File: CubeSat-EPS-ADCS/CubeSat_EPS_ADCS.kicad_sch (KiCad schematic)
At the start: 18 parts, among them J1 Conn_01x02_Pin, J2 Conn_01x03_Pin, J3 Conn_01x08_Pin, J4 Conn_01x02_Pin, J5 Screw_Terminal_01x02, J6 Screw_Terminal_01x02, J7 Screw_Terminal_01x02, U1 DRV8833 Module, U2 DRV8833 Module, U4 Buck_LM2596

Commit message: Mostly fine tuning the boards, also added capacitor for battery ADC
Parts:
- removed R1, R2, R3, R4, R5, R6: 10K, Resistor_THT:R_Axial_DIN0207_L6.3mm_D2.5mm_P7.62mm_Horizontal, symbol Device:R
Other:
- note removed: "PULL DOWN RESISTORS"

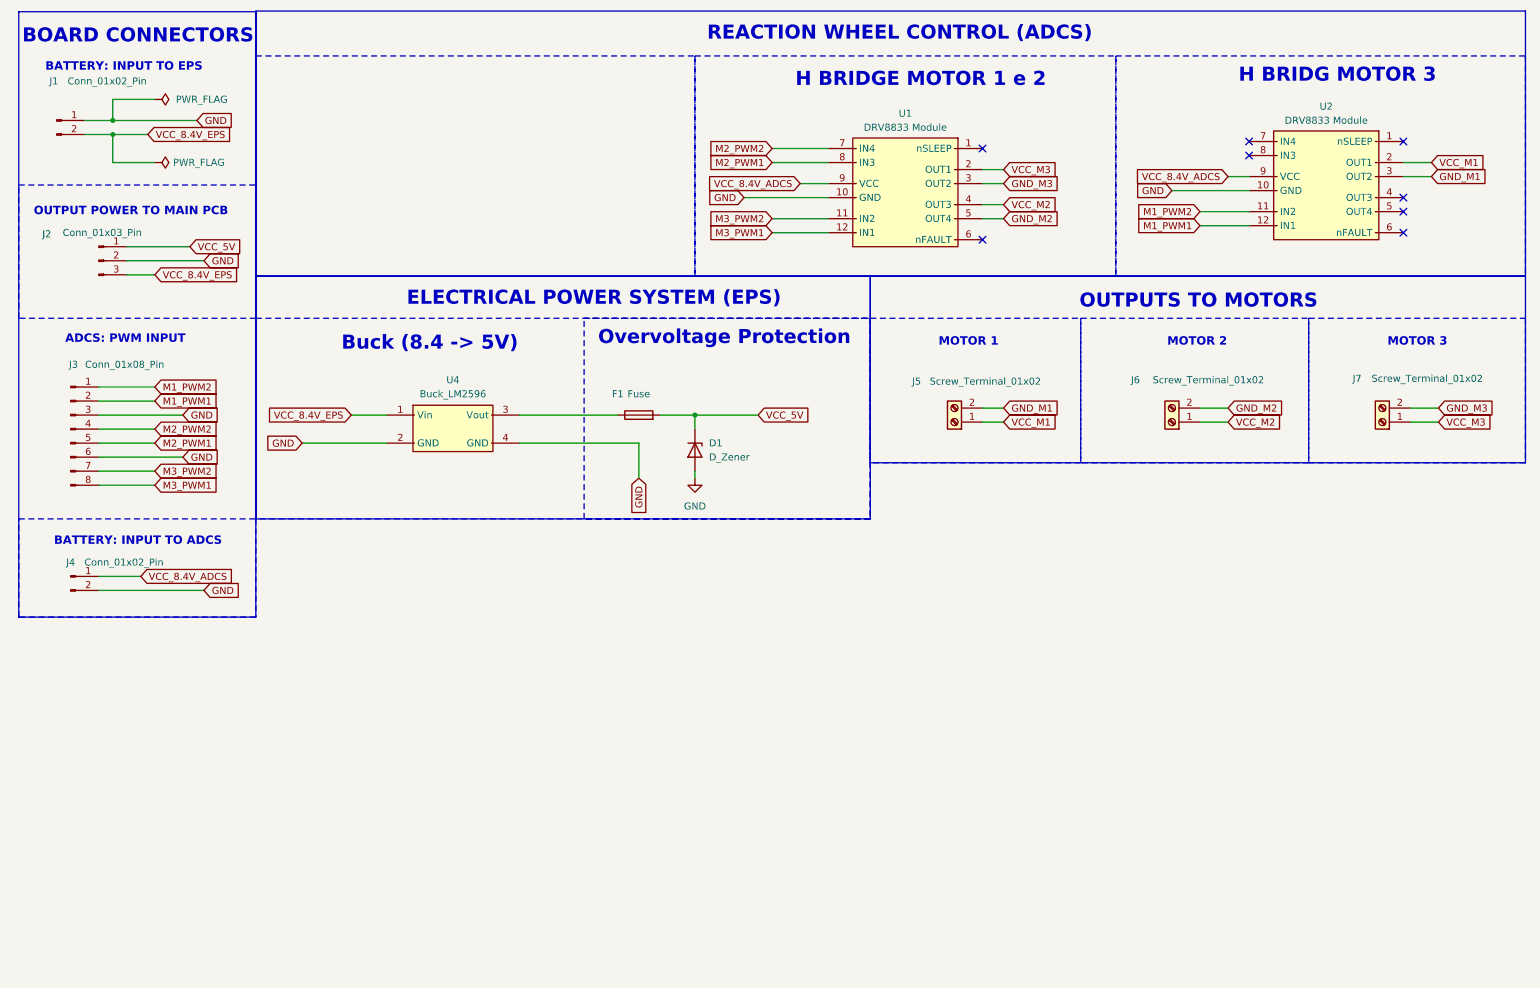
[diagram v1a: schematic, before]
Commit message: Changing the size of all traces to fit the 1 mm requirement of the draft PCB
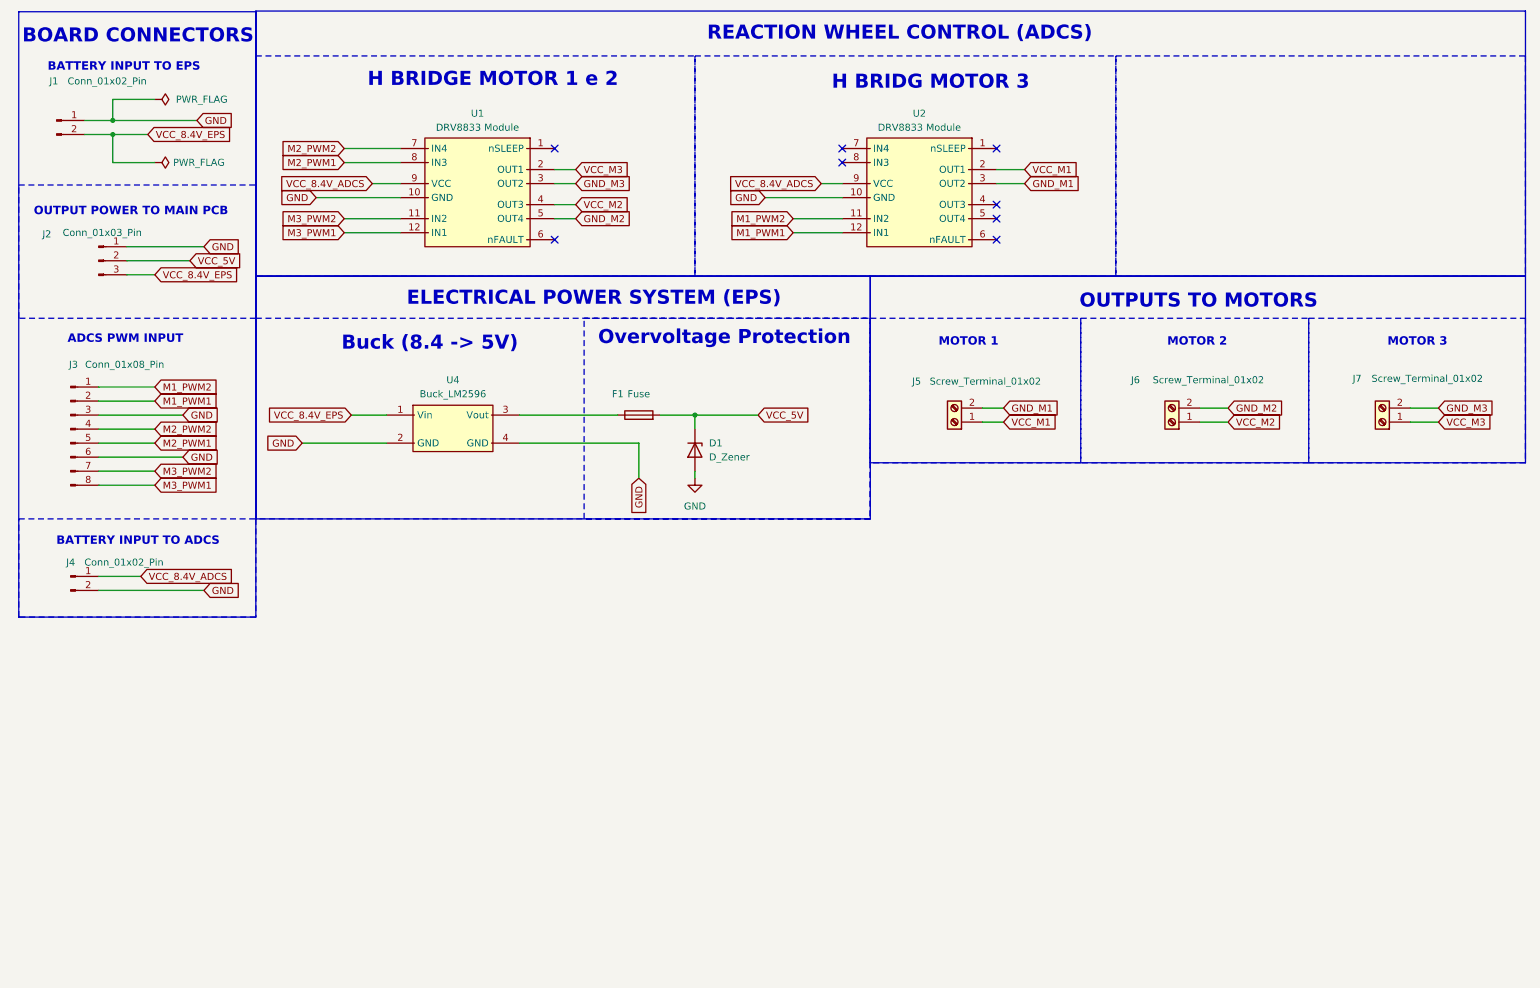
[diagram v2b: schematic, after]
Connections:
- net GND: now also J2.1 (Pin_1); no longer J2.2 (Pin_2)
- net VCC_5V: now also J2.2 (Pin_2); no longer J2.1 (Pin_1)
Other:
- note added: "ADCS PWM INPUT"
- note added: "BATTERY INPUT TO ADCS"
- note added: "BATTERY INPUT TO EPS"
- note removed: "ADCS: PWM INPUT"
- note removed: "BATTERY: INPUT TO ADCS"
- note removed: "BATTERY: INPUT TO EPS"
- moved on the sheet: U1, U2

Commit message: final version of the 3 PCBs, minor size changes for the protoypes
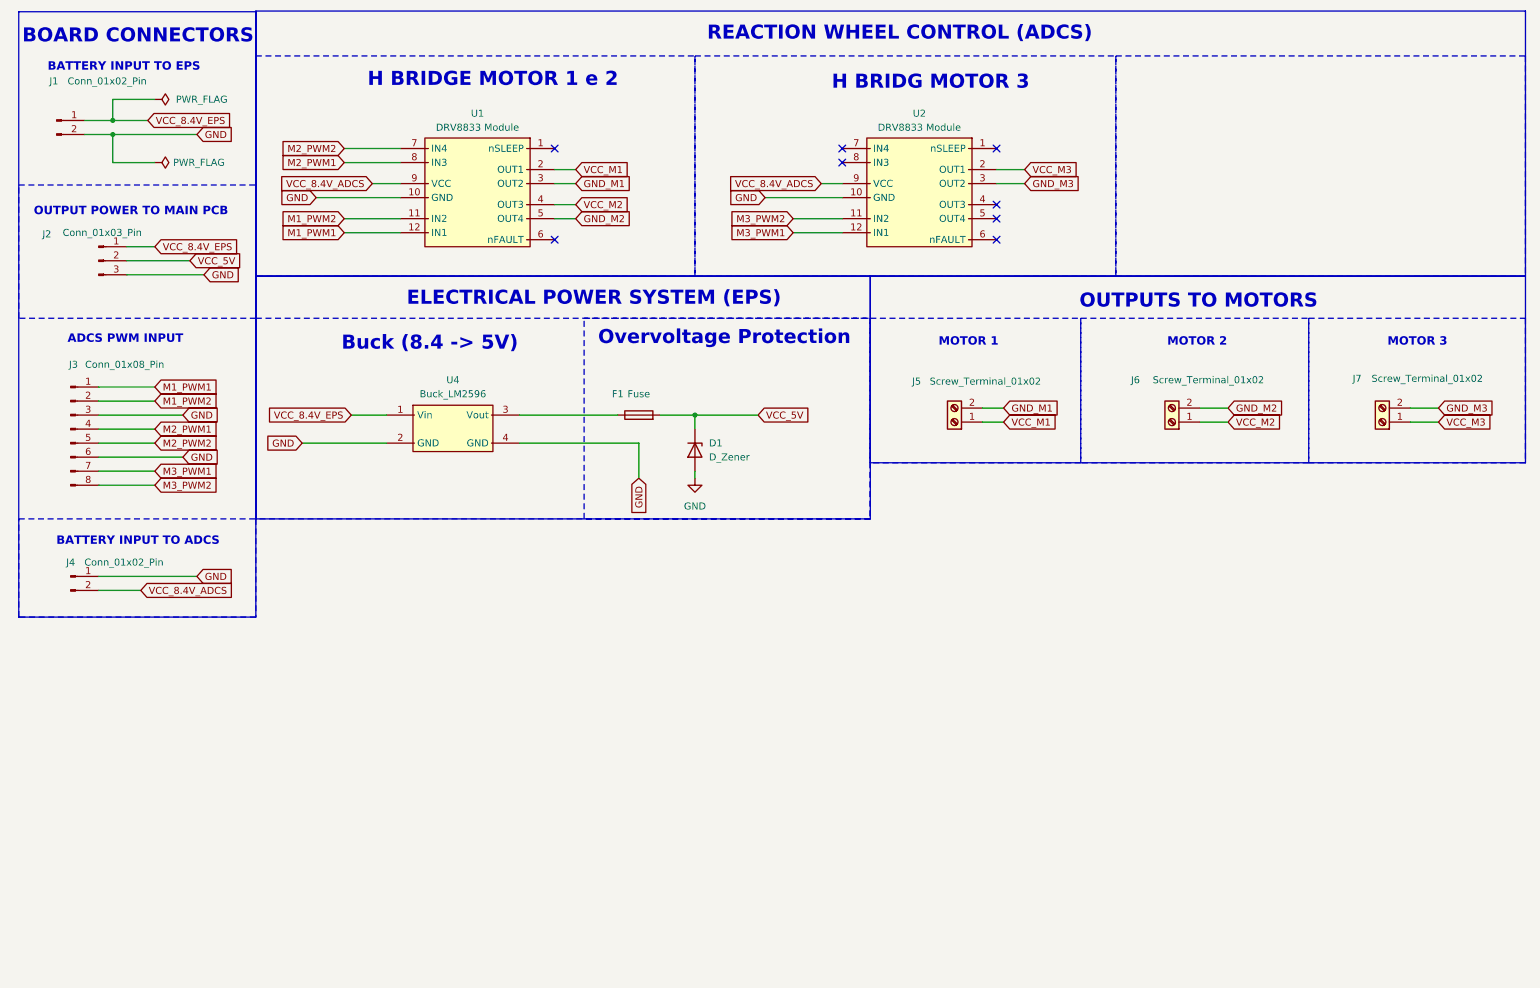
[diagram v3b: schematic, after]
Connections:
- net GND: now also J1.2 (Pin_2), J2.3 (Pin_3), J4.1 (Pin_1); no longer J1.1 (Pin_1), J2.1 (Pin_1), J4.2 (Pin_2)
- net GND_M1: now also U1.3 (OUT2); no longer U2.3 (OUT2)
- net GND_M3: now also U2.3 (OUT2); no longer U1.3 (OUT2)
- net M1_PWM1: now also J3.1 (Pin_1), U1.12 (IN1); no longer J3.2 (Pin_2), U2.12 (IN1)
- net M1_PWM2: now also J3.2 (Pin_2), U1.11 (IN2); no longer J3.1 (Pin_1), U2.11 (IN2)
- net M2_PWM1: now also J3.4 (Pin_4); no longer J3.5 (Pin_5)
- net M2_PWM2: now also J3.5 (Pin_5); no longer J3.4 (Pin_4)
- net M3_PWM1: now also J3.7 (Pin_7), U2.12 (IN1); no longer J3.8 (Pin_8), U1.12 (IN1)
- net M3_PWM2: now also J3.8 (Pin_8), U2.11 (IN2); no longer J3.7 (Pin_7), U1.11 (IN2)
- net VCC_8.4V_ADCS: now also J4.2 (Pin_2); no longer J4.1 (Pin_1)
- net VCC_8.4V_EPS: now also J1.1 (Pin_1), J2.1 (Pin_1); no longer J1.2 (Pin_2), J2.3 (Pin_3)
- net VCC_M1: now also U1.2 (OUT1); no longer U2.2 (OUT1)
- net VCC_M3: now also U2.2 (OUT1); no longer U1.2 (OUT1)

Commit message: add new drill format
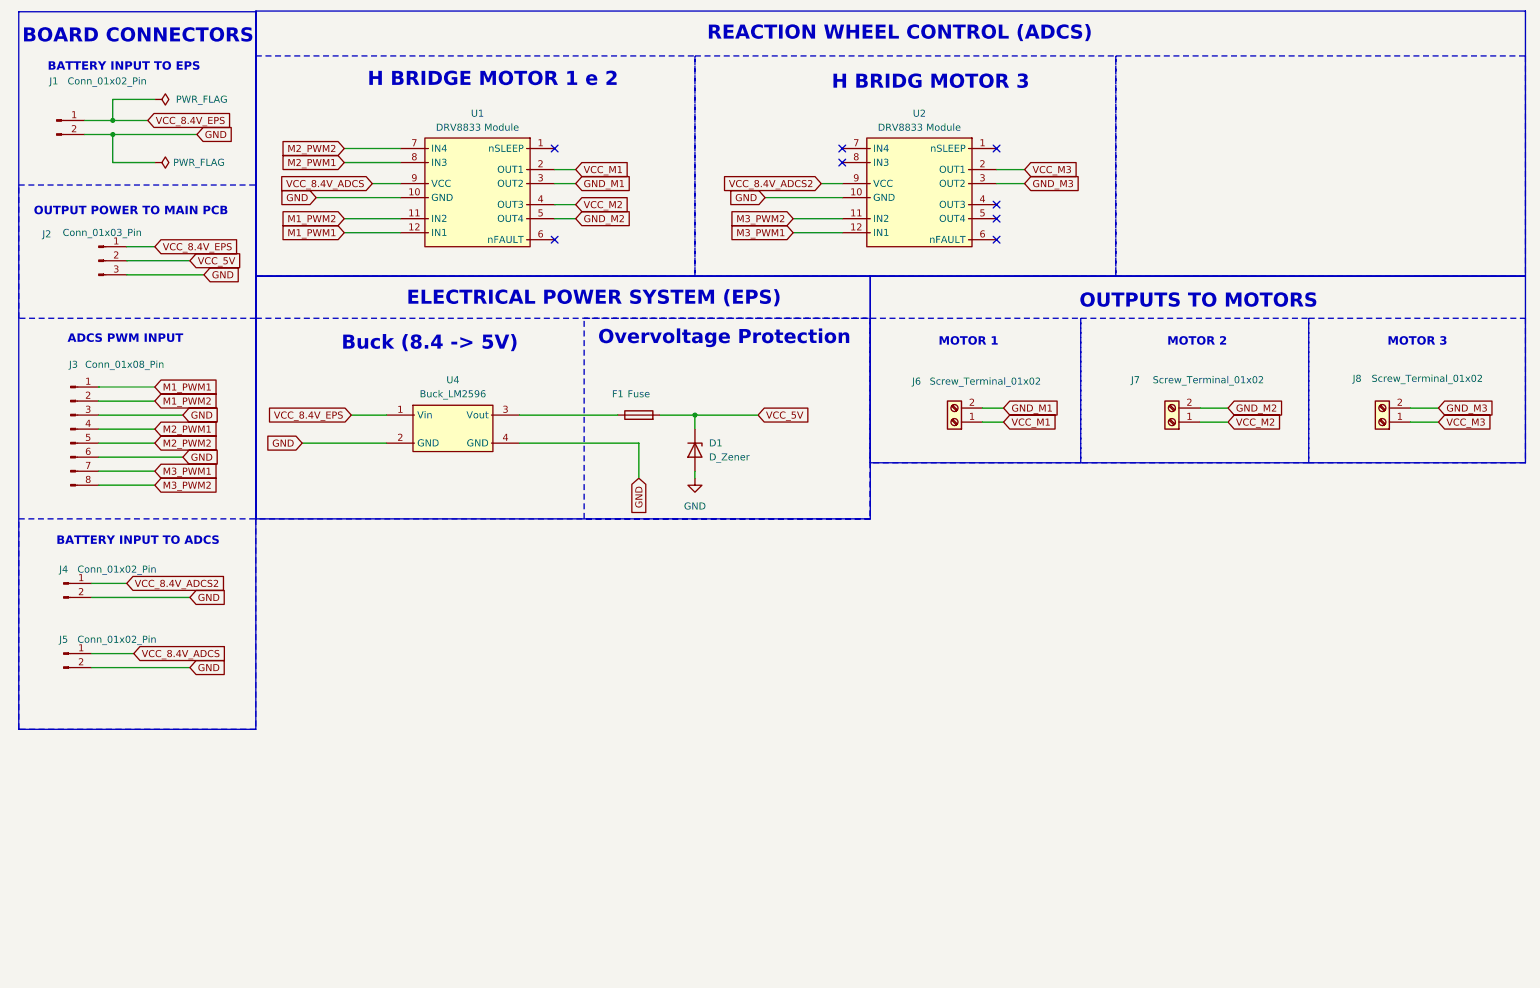
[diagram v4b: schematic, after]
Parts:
- added J4: Conn_01x02_Pin, Connector_JST:JST_EH_B2B-EH-A_1x02_P2.50mm_Vertical, symbol Connector:Conn_01x02_Pin
- renumbered J4 to J5, J5 to J6, J6 to J7, J7 to J8
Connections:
- net GND: now also J5.2 (Pin_2), J4.2 (Pin_2); no longer J5.1 (Pin_1)
- net VCC_8.4V_ADCS: now also J5.1 (Pin_1); no longer J5.2 (Pin_2), U2.9 (VCC)
- new net VCC_8.4V_ADCS2: J4.1 (Pin_1), U2.9 (VCC)
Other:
- moved on the sheet: J5

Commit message: final changes in ALL 3 pcbs: mounting wholes config, and a few connector changes
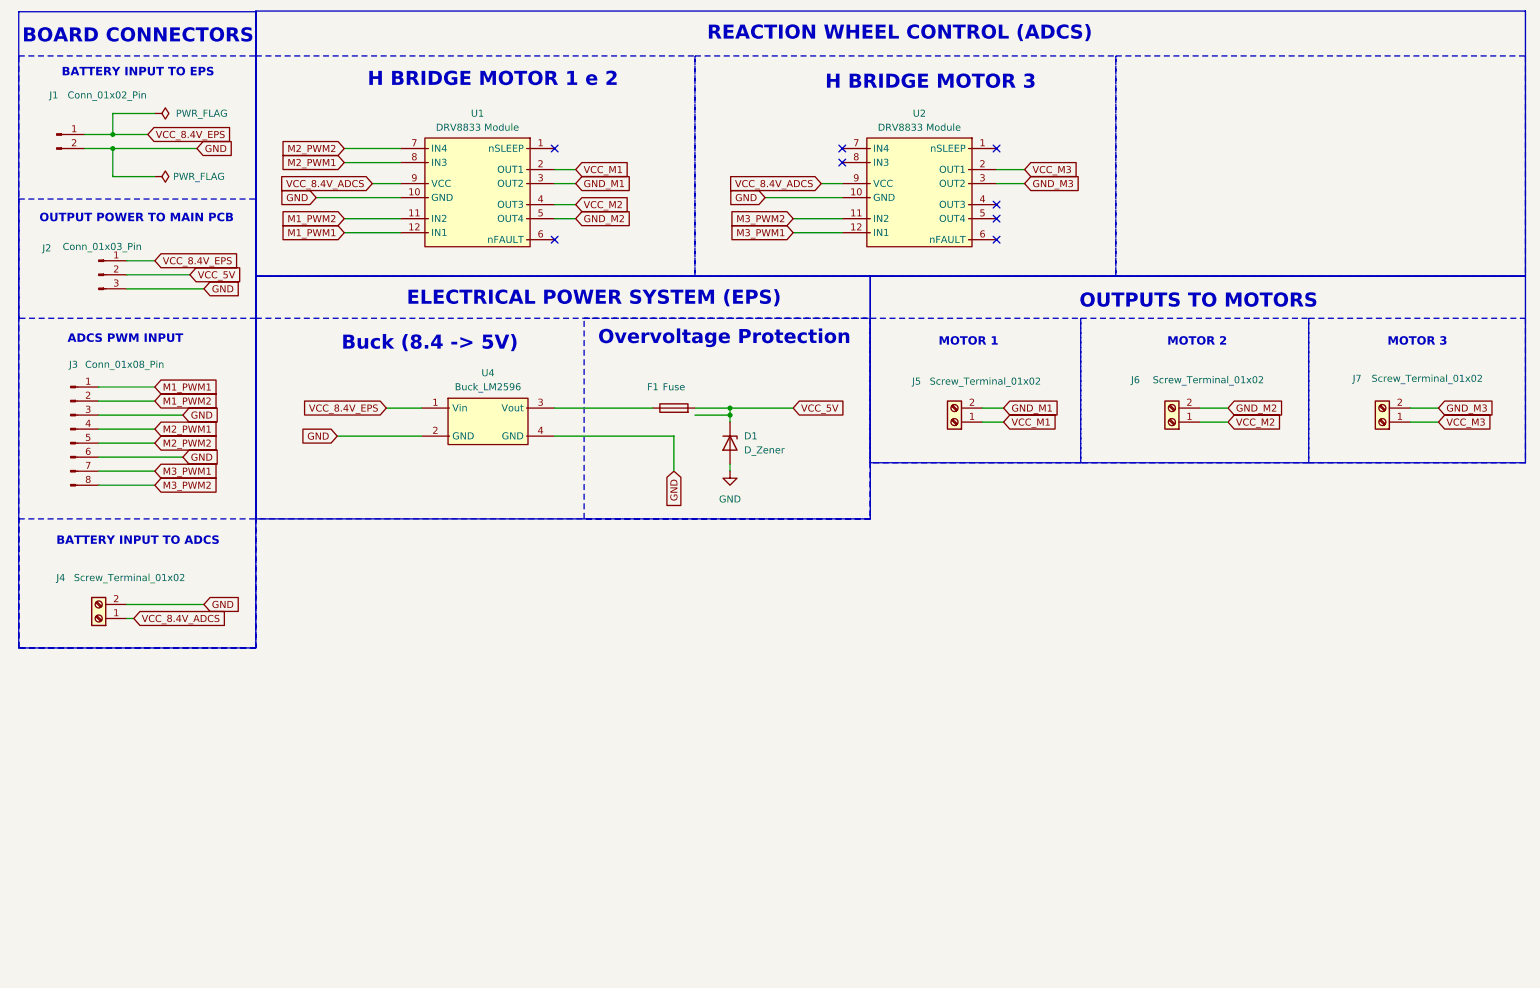
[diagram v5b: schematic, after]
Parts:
- removed J4, J5: Conn_01x02_Pin, Connector_JST:JST_EH_B2B-EH-A_1x02_P2.50mm_Vertical, symbol Connector:Conn_01x02_Pin
- added J4: Screw_Terminal_01x02, TerminalBlock_Phoenix:TerminalBlock_Phoenix_MKDS-1,5-2_1x02_P5.00mm_Horizontal, symbol Connector:Screw_Terminal_01x02
- renumbered J6 to J5, J7 to J6, J8 to J7
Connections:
- net VCC_8.4V_ADCS2 is gone; now on net VCC_8.4V_ADCS: U2.9 (VCC)
- net GND: now also J4.2 (Pin_2)
- net VCC_8.4V_ADCS: now also J4.1 (Pin_1)
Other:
- note added: "H BRIDGE MOTOR 3"
- note removed: "H BRIDG MOTOR 3"
- moved on the sheet: D1, F1, J1, J2, U4

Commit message: last minute changes, adding kill swithc and backup buck converter for the motors
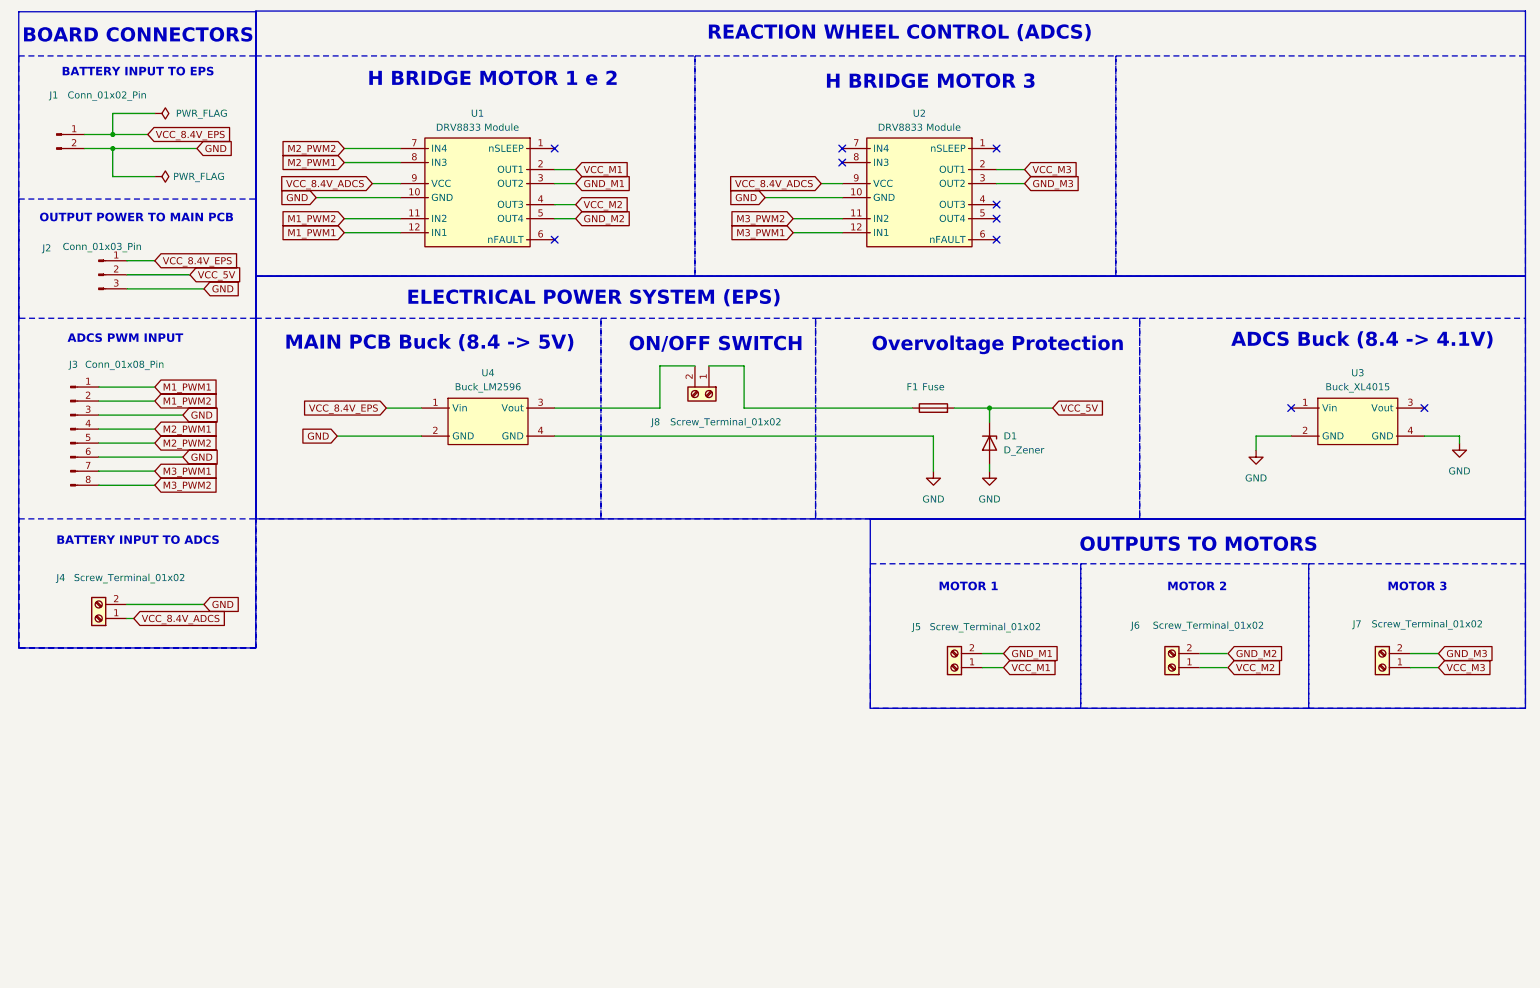
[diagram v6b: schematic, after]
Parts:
- added J8: Screw_Terminal_01x02, TerminalBlock_Phoenix:TerminalBlock_Phoenix_MKDS-1,5-2_1x02_P5.00mm_Horizontal, symbol Connector:Screw_Terminal_01x02
- added U3: Buck_XL4015, Cubesat_Modules:Buck_XL4015, symbol Cubesat_Modules:Buck_XL4015
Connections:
- net GND: now also U3.2 (GND), U3.4 (GND)
- net at F1.1: now also J8.1 (Pin_1); no longer U4.3 (Vout)
- new net: J8.2 (Pin_2), U4.3 (Vout)
- no-connect marks 8 -> 10
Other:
- note added: "ADCS Buck (8.4 -> 4.1V)"
- note added: "MAIN PCB Buck (8.4 -> 5V)"
- note added: "ON/OFF SWITCH"
- note removed: "Buck (8.4 -> 5V)"
- moved on the sheet: D1, F1, J5, J6, J7
